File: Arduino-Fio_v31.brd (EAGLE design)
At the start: 102 x 63.5 mm, 56 parts, among them U1 MCP73831, U5 ATMEGA32U4, U6 MIC5219-3.3, X1 MJ4435-R1503_03, X2 USB_MICROB_PLUGCONN-11752, Y2 8MHz

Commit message: V 0.11 now with SD card slot
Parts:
- added U$3: MICROSD, adafruit:MICROSD
- moved PAD6 42.4 mm to (56.5, 9.53), turned to 0 degrees
- moved PAD5 41.2 mm to (59.1, 9.53), turned to 0 degrees
- moved PAD4 40.3 mm to (61.6, 9.53), turned to 0 degrees
- moved PAD3 39.8 mm to (64.1, 9.53), turned to 0 degrees
- moved PAD1 39.6 mm to (69.2, 9.53), turned to 0 degrees
- moved PAD2 39.5 mm to (66.7, 9.53), turned to 0 degrees
- moved D4 39.4 mm to (42.5, 37.5)
- moved R9 37.0 mm to (42.5, 31.8), turned to 90 degrees
- moved C5 32.2 mm to (63.3, 21.1)
- moved R13 31.9 mm to (46.4, 31.8)
- moved Y2 31.1 mm to (62.5, 26.4), turned to 270 degrees
- moved C7 30.3 mm to (61.4, 21.1)
- moved LED1 22.7 mm to (46.4, 37.5)
- moved JP4 20.3 mm to (82.6, 15.7)
- moved U5 15.2 mm to (70.9, 19.2), turned to 222 degrees
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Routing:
- net GND: track 0.00 -> 47.0 mm, vias 0 -> 2
- net VBATT: track 0.00 -> 17.7 mm
- net 3.3V: track 0.00 -> 13.8 mm
- net N$11: track 0.00 -> 6.13 mm
- net VBATT_LVL: track 0.00 -> 5.17 mm
- net N$9: track 0.00 -> 2.74 mm
- net USB_VCC: track 0.00 -> 2.54 mm
- added copper zone on layer 16, net GND
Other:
- outline, holes or cut-outs redrawn

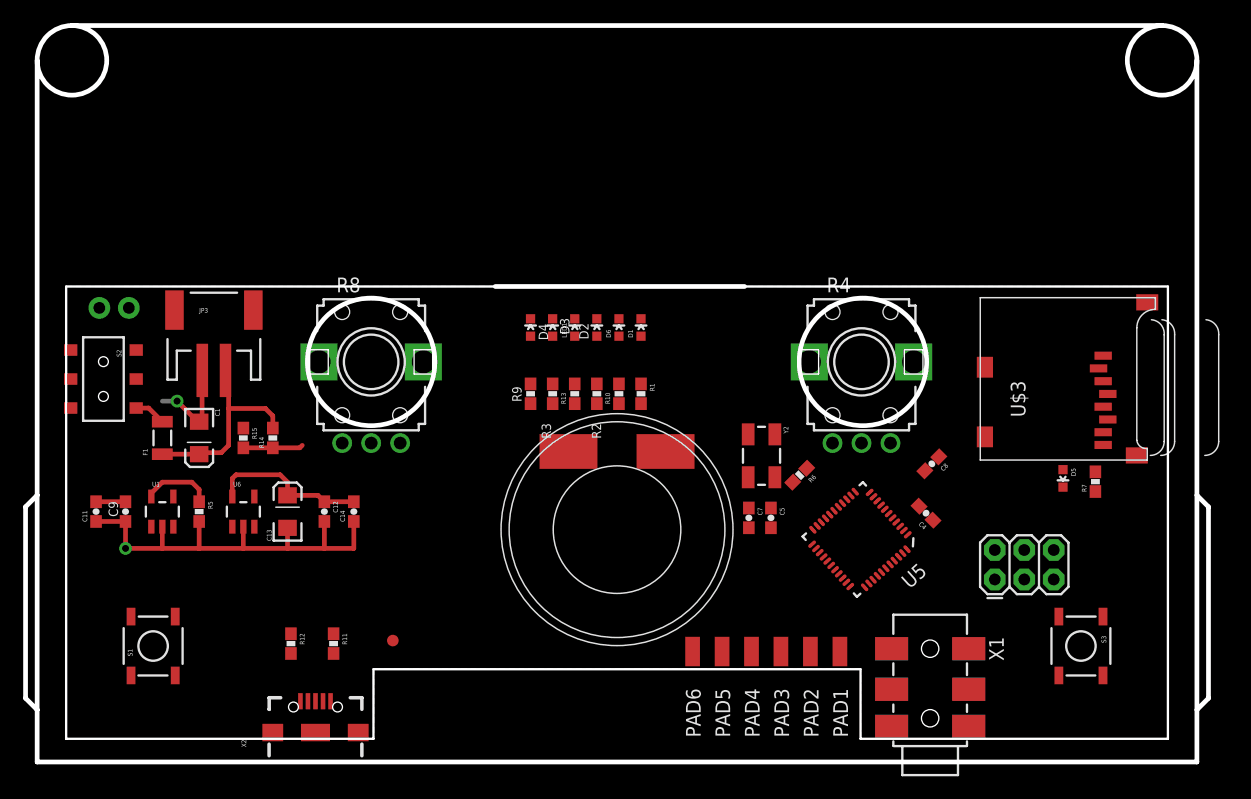
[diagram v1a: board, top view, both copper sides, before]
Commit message: Finished Routing
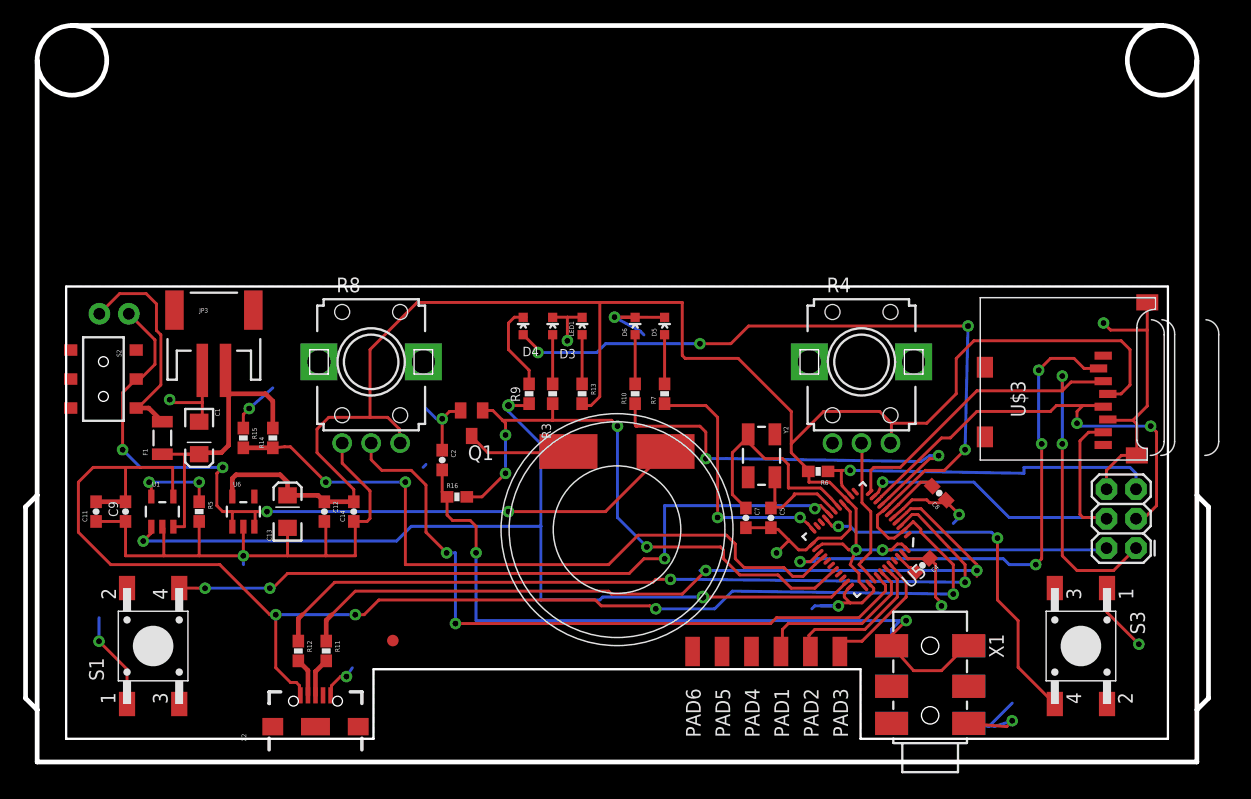
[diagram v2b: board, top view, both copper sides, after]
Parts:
- removed D1: Yellow, SparkFun:LED-0603
- removed D2: Green, SparkFun:LED-0603
- removed R1, R2: 330, SparkFun-Resistors:0603-RES
- added C2: 1uF, SparkFun-Capacitors:0603-CAP
- added Q1: BSS123, transistor-small-signal:SOT23
- added R16: 330, SparkFun-Resistors:0603-RES
- S1, S3: device SparkFun:TACTILE_SWITCH_SMD -> Gaudi:TASTER-9314_SMD
- moved R7 37.9 mm to (54.1, 31.8)
- moved D5 36.8 mm to (54.1, 37.6), turned to 0 degrees
- moved JP4 12.5 mm to (94.8, 18.4), turned to 90 degrees
- moved PAD1 5.08 mm to (64.1, 9.53)
- moved PAD3 5.08 mm to (69.2, 9.53)
- moved C4 4.51 mm to (76.3, 17.0), turned to 225 degrees
- moved C8 2.60 mm to (77.8, 23.2), turned to 135 degrees
- moved R6 1.62 mm to (67.3, 25.1), turned to 180 degrees
- moved D6 1.40 mm to (51.6, 37.6)
- moved R10 1.40 mm to (51.6, 31.8)
- moved R11 0.90 mm to (24.9, 9.57)
- moved R12 0.90 mm to (22.5, 9.57)
- moved D4 0.65 mm to (41.9, 37.6)
- moved LED1 0.65 mm to (47.0, 37.6)
- moved R13 0.64 mm to (47.0, 31.8), turned to 270 degrees
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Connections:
- removed net ASSOCIATE: R1.2
- removed net N$12: R3.2, U$1.1
- removed net N$2: D1.A, R1.1
- removed net N$3: D2.A, R2.1
- removed net N$4: R2.2
- new net N$13: Q1.3, U$1.2
- new net N$21: C2.2, R16.1, X1.3, X1.33, X1.33B
- net 3.3V: now also R4.3, R8.3, U$3.4
- net A0: now also R4.2
- net A1: now also R8.2
- net A2: now also PAD1.1
- net A3: now also PAD2.1
- net A4: now also PAD3.1
- net D2: now also S3.4
- net D3: now also S1.4
- net D4: now also U$3.2
- net D9: now also Q1.1, R16.2, R3.2
- net GND: now also C2.1, Q1.2, R4.1, R8.1, U$3.6, U$3.MT1, U$3.MT2, X1.1, X1.11B, X1.1B; no longer D1.C, D2.C, U$1.2
- net MISO: now also U$3.3
- net MOSI: now also U$3.7
- net RAW: now also U$1.1
- net SCK: now also U$3.5
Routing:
- net USB_VCC: track 2.54 -> 183.1 mm, vias 0 -> 8
- net 3.3V: track 13.8 -> 181.4 mm, vias 0 -> 2
- net GND: track 47.0 -> 180.2 mm, vias 2 -> 15
- net CHARGE_STAT: track 0.00 -> 83.4 mm, vias 0 -> 3
- net RAW: track 0.00 -> 71.7 mm, vias 0 -> 4
- net D+: track 0.00 -> 70.8 mm, vias 0 -> 2
- net D-: track 0.00 -> 70.2 mm, vias 0 -> 2
- net N$21: track 0.00 -> 65.8 mm, vias 0 -> 2
- net D3: track 0.00 -> 62.2 mm, vias 0 -> 4
- net A1: track 0.00 -> 60.3 mm, vias 0 -> 2
- net VBATT_LVL: track 5.17 -> 62.3 mm, vias 0 -> 2
- net D9: track 0.00 -> 52.7 mm, vias 0 -> 4
- net MISO: track 0.00 -> 49.6 mm, vias 0 -> 2
- net D4: track 0.00 -> 45.8 mm, vias 0 -> 4
- net SCK: track 0.00 -> 40.4 mm, vias 0 -> 2
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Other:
- outline, holes or cut-outs redrawn
